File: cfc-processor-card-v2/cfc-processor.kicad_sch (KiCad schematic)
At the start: 6 parts

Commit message: CFC processor schematic Change
changed to hierarchy view, changed all global net labels to hierarchy labels, changed all resistor, capacitor, and ground symbols to modern oresat labels. Deleted connectors sheet and added .history to gitignore.
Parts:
- added J1: TFM-120-01-L-D-RA, oresat-connectors:J-SAMTEC-TFM-120-X1-XXX-D-RA, symbol oresat-connectors:J-SAMTEC-TFM-120-01-L-D-RA
- added J2: 2-1734592-0, oresat-connectors:J-JST-SM14BSHLSTF, symbol oresat-connectors:ORESAT-DEBUG-CONNECTOR-3
- added J3: J-SAMTEC-TFM-110-X1-XXX-D-RA, oresat-connectors:J-SAMTEC-TFM-110-X1-XXX-D-RA, symbol oresat-connectors:J-SAMTEC-TFM-110-01-L-D-RA
- added PCB1: ORESAT-CARD-V1.3-GENERIC-0RF, cfc-card:ORESAT-CARD-V1.3-GENERIC-0RF, symbol cfc-card-eagle-import:ORESAT-CARD-V1.3-GENERIC-0RF
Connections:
- new net: J1.33, J1.34
- new net: J1.35, J1.36
- new net: J1.39, J1.40
- new net C3-UART-RX: J1.38
- new net C3-UART-TX: J1.37
- new net CAN2_H: J1.17, J1.18
- new net CAN2_L: J1.19, J1.20
- new net GND: J1.27, J1.28, J1.29, J1.30, J2.14 (GND), J2.15 (PAD), J2.16 (PAD), J2.5 (GND)
- new net OPD_PWR: J1.15, J1.16
- new net OPD_SCL: J1.13, J1.14
- new net OPD_SDA: J1.11, J1.12
- new net OSD3358: SIP A (PWR)/NRESET: J2.10 (NRST)
- new net OSD3358: SIP B/THERM+: J3.11, J3.12
- new net OSD3358: SIP B/USB_CLI_N: J2.4 (DEVICE-D-)
- new net OSD3358: SIP B/USB_CLI_P: J2.3 (DEVICE-D+)
- new net OSD3358: SIP B/USB_CLI_VBUS: J2.1 (VBUSP), J2.2 (VBUSP)
- new net OSD3358: SIP C/UART-RX: J2.7 (CARD-RX)
- new net OSD3358: SIP C/UART-TX: J2.6 (CARD-TX)
- new net OUT1_N: J3.5, J3.6, J3.7, J3.8
- new net SENSOR_ENABLE: J3.13, J3.14
- new net SPI1_CLK: J3.17, J3.18
- new net SPI1_MISO: J3.15, J3.16
- new net SPI1_MOSI: J3.19, J3.20
- new net TEC_ENABLE: J3.10, J3.9
- new net TXCLK_N: J3.1, J3.2
- new net TXCLK_P: J3.3, J3.4
- new net VBUS: J1.23, J1.24, J1.25, J1.26
- no-connect marks 0 -> 19
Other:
- sheet Connectors renamed Deserializer
- sheet OSD3358: SIP B (USB, XTAL, ADC) renamed OSD3358: SIP B
- sheet OSD3358: SIP C (SD, eMMC, PRU) renamed OSD3358: SIP C
- sheet Deserializer: file cfc-processor-sch-connectors.kicad_sch -> cfc-processor-sch-Deserializer.kicad_sch
- sheet Deserializer ports: added OUT1_N, OUT1_P, PRU_BUS.PRU0_0, PRU_BUS.PRU0_1, PRU_BUS.PRU0_2, PRU_BUS.PRU0_3, PRU_BUS.PRU0_4, PRU_BUS.PRU0_5, PRU_BUS.PRU0_6, PRU_BUS.PRU_16_CLK, TXCLK_N, TXCLK_P; removed none
- sheet OSD3358: SIP A (PWR) ports: added NRESET, VIN_USB; removed none
- sheet OSD3358: SIP B ports: added THERM+, USB_CLI_N, USB_CLI_P, USB_CLI_VBUS, VIN_USB; removed none
- sheet OSD3358: SIP C ports: added CAN2_H, CAN2_L, PRU_BUS.PRU0_0, PRU_BUS.PRU0_1, PRU_BUS.PRU0_2, PRU_BUS.PRU0_3, PRU_BUS.PRU0_4, PRU_BUS.PRU0_5, PRU_BUS.PRU0_6, PRU_BUS.PRU_16_CLK, SPI1_CLK, SPI1_MISO, SPI1_MOSI, UART-RX, UART-TX; removed none
- sheet OSD3358: SIP D (BOOT) ports: added SENSOR_ENABLE, SYSBOOT2, TEC_ENABLE; removed none
- sheet Power (OPD) ports: added C3-UART-RX, C3-UART-TX, OPD_PWR, OPD_SCL, OPD_SDA, SYSBOOT2, UART0_RX, UART0_TX; removed none
- note added: "Aux Bus Connector"
- note added: "CAN1_H"
- note added: "CAN1_L"
- note added: "Main Bus Connector"
- note added: "Oresat Debug Connector"
- note added: "SPARE1"
- note added: "SPARE10"
- note added: "SPARE2"
- note added: "SPARE21"
- note added: "SPARE22"
- note added: "SPARE3"
- note added: "SPARE31"
- note added: "SPARE32"
- note added: "SPARE4"
- note added: "SPARE5"
- note added: "SPARE6"
- note added: "SPARE7"
- note added: "SPARE8"
- note added: "SPARE9"
- note added: "~{SD}"
- moved on the sheet: FID1, FID2, FID3, FID4, FID5, FID6

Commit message: Updated OPD
couple of resistors and caps added to schematic. Changed USB ESD clamp VDD to 3.3v instead of octavo created VDD line.
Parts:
- removed PCB1: ORESAT-CARD-V1.3-GENERIC-0RF, cfc-card:ORESAT-CARD-V1.3-GENERIC-0RF, symbol cfc-card-eagle-import:ORESAT-CARD-V1.3-GENERIC-0RF
- added C56: 10u, oresat-passives:0805-B-NOSILK, symbol Device:C
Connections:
- net GND: now also C56.2
- net VBUS: now also C56.1
- net OSD3358: SIP B/THERM+ renamed THERM+
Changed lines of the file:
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@@
+	)
+	(junction
+		(at 58.42 100.33)
+		(diameter 0)
+		(color 0 0 0 0)
 	)
 	(junction
@@
 	)
 	(junction
+		(at 58.42 90.17)
+		(diameter 0)
+		(color 0 0 0 0)
+	)
+	(junction
 		(at 46.99 90.17)
 		(diameter 0)
@@
 	(wire
 		(pts
+			(xy 58.42 99.06) (xy 58.42 100.33)
+		)
+		(stroke
+			(width 0)
+			(type default)
+		)
+	)
+	(wire
+		(pts
 			(xy 388.62 139.7) (xy 392.43 139.7)
 		)
@@
 	(wire
 		(pts
-			(xy 317.5 132.08) (xy 354.33 132.08)
-		)
-		(stroke
-			(width 0)
-			(type default)
-		)
-	)
-	(wire
-		(pts
-			(xy 321.31 175.26) (xy 321.31 137.16)
+			(xy 316.23 132.08) (xy 354.33 132.08)
+		)
+		(stroke
+			(width 0)
+			(type default)
+		)
+	)
+	(wire
+		(pts
+			(xy 318.77 175.26) (xy 318.77 137.16)
 		)
 		(stroke
@@
 	(wire
 		(pts
-			(xy 325.12 142.24) (xy 356.87 142.24)
+			(xy 321.31 142.24) (xy 356.87 142.24)
 		)
 		(stroke
@@
 	(wire
 		(pts
-			(xy 307.34 175.26) (xy 321.31 175.26)
+			(xy 307.34 175.26) (xy 318.77 175.26)
 		)
 		(stroke
@@
 	(wire
 		(pts
-			(xy 325.12 177.8) (xy 325.12 142.24)
+			(xy 321.31 177.8) (xy 321.31 142.24)
 		)
 		(stroke
@@
 	(wire
 		(pts
-			(xy 307.34 177.8) (xy 325.12 177.8)
+			(xy 307.34 177.8) (xy 321.31 177.8)
 		)
 		(stroke
@@
 	(wire
 		(pts
+			(xy 58.42 90.17) (xy 58.42 91.44)
+		)
+		(stroke
+			(width 0)
+			(type default)
+		)
+	)
+	(wire
+		(pts
 			(xy 39.37 208.28) (xy 50.8 208.28)
 		)
@@
 	(wire
 		(pts
-			(xy 307.34 172.72) (xy 317.5 172.72)
+			(xy 307.34 172.72) (xy 316.23 172.72)
 		)
 		(stroke
@@
 	(wire
 		(pts
-			(xy 321.31 137.16) (xy 356.87 137.16)
+			(xy 318.77 137.16) (xy 356.87 137.16)
 		)
 		(stroke
@@
 	(wire
 		(pts
-			(xy 317.5 172.72) (xy 317.5 132.08)
-		)
-		(stroke
-			(width 0)
-			(type default)
+			(xy 316.23 172.72) (xy 316.23 132.08)
+		)
+		(stroke
+			(width 0)
+			(type default)
+		)
+	)
+	(label "THERM+"
+		(at 379.73 152.4 0)
+		(effects
+			(font
+				(size 1.27 1.27)
+			)
+			(justify left bottom)
 		)
 	)
 	(label "TEC_ENABLE"
-		(at 375.92 147.32 0)
+		(at 374.65 147.32 0)
 		(effects
 			(font
@@
 	)
 	(label "SPI1_MISO"
-		(at 377.19 162.56 0)
+		(at 375.92 162.56 0)
 		(effects
 			(font
@@
 	)
 	(label "SPI1_MOSI"
-		(at 377.19 172.72 0)
+		(at 375.92 172.72 0)
 		(effects
 			(font
@@
 	)
 	(symbol
+		(lib_id "Device:C")
+		(at 58.42 95.25 0)
+		(mirror y)
+		(unit 1)
+		(body_style 1)
+		(exclude_from_sim no)
+		(in_bom yes)
+		(on_board yes)
+		(in_pos_files yes)
+		(dnp no)
+		(property "Reference" "C56"
+			(at 65.024 94.996 0)
+			(show_name no)
+			(do_not_autoplace no)
+			(effects
+				(font
+					(size 1.27 1.27)
+				)
+				(justify left bottom)
+			)
+		)
+		(property "Value" "10u"
+			(at 65.024 97.028 0)
+			(show_name no)
+			(do_not_autoplace no)
+			(effects
+				(font
+					(size 1.27 1.27)
+				)
+				(justify left bottom)
+			)
+		)
+		(property "Footprint" "oresat-passives:0805-B-NOSILK"
+			(at 58.42 95.25 0)
+			(hide yes)
+			(show_name no)
+			(do_not_autoplace no)
+			(effects
+				(font
+					(size 1.27 1.27)
+				)
+			)
+		)
+		(property "Datasheet" "https://mm.digikey.com/Volume0/opasdata/d220001/medias/docus/7851/1276_CL21B1.pdf"
+			(at 58.42 95.25 0)
+			(hide yes)
+			(show_name no)
+			(do_not_autoplace no)
+			(effects
+				(font
+					(size 1.27 1.27)
+				)
+			)
+		)
+		(property "Description" "10 µF ±10% 25V Ceramic Capacitor X7R 0805 (2012 Metric)"
+			(at 58.42 95.25 0)
+			(hide yes)
+			(show_name no)
+			(do_not_autoplace no)
+			(effects
+				(font
+					(size 1.27 1.27)
+				)
+			)
+		)
+		(property "DIS" "DigiKey"
+			(at 58.42 95.25 0)
+			(hide yes)
+			(show_name no)
+			(do_not_autoplace no)
+			(effects
+				(font
+					(size 1.27 1.27)
+				)
+			)
+		)
+		(property "DPN" "1276-CL21B106KAYQNNETR-ND"
+			(at 58.42 95.25 0)
+			(hide yes)
+			(show_name no)
+			(do_not_autoplace no)
+			(effects
+				(font
+					(size 1.27 1.27)
+				)
+			)
+		)
+		(property "MFR" "Samsung Electro-Mechanics"
+			(at 58.42 95.25 0)
+			(hide yes)
+			(show_name no)
+			(do_not_autoplace no)
+			(effects
+				(font
+					(size 1.27 1.27)
+				)
+			)
+		)
+		(property "MPN" "CL21B106KAYQNNE"
+			(at 58.42 95.25 0)
+			(hide yes)
+			(show_name no)
+			(do_not_autoplace no)
+			(effects
+				(font
+					(size 1.27 1.27)
+				)
+			)
+		)
+		(pin "1"
+		)
+		(pin "2"
+		)
+		(instances
+			(project "cfc-processor"
+				(path "/07ac832f-8d98-4777-b655-1877592dfd88"
+					(reference "C56")
+					(unit 1)
+				)
+			)
+		)
+	)
+	(symbol
 		(lib_name "Fiducial_4")
 		(lib_id "Mechanical:Fiducial")
@@
 					(unit 1)
 				)
-			)
-		)
-	)
-	(symbol
-		(lib_id "cfc-card-eagle-import:ORESAT-CARD-V1.3-GENERIC-0RF")
-		(at 16.51 248.92 0)
-		(unit 1)
-		(body_style 1)
-		(exclude_from_sim no)
-		(in_bom yes)
-		(on_board yes)
-		(in_pos_files yes)
-		(dnp no)
-		(property "Reference" "PCB1"
-			(at 16.51 248.92 0)
-			(hide yes)
-			(show_name no)
-			(do_not_autoplace no)
-			(effects
-				(font
-					(size 1.27 1.27)
-				)
-			)
-		)
-		(property "Value" "ORESAT-CARD-V1.3-GENERIC-0RF"
-			(at 16.51 248.92 0)
-			(hide yes)
-			(show_name no)
-			(do_not_autoplace no)
-			(effects
-				(font
-					(size 1.27 1.27)
-				)
-			)
-		)
-		(property "Footprint" "cfc-card:ORESAT-CARD-V1.3-GENERIC-0RF"
-			(at 16.51 248.92 0)
-			(hide yes)
-			(show_name no)
-			(do_not_autoplace no)
-			(effects
-				(font
-					(size 1.27 1.27)
-				)
-			)
-		)
-		(property "Datasheet" "N/A"
-			(at 16.51 248.92 0)
-			(hide yes)
-			(show_name no)
-			(do_not_autoplace no)
-			(effects
-				(font
-					(size 1.27 1.27)
-				)
-			)
-		)
-		(property "Description" "N/A"
-			(at 16.51 248.92 0)
-			(hide yes)
-			(show_name no)
-			(do_not_autoplace no)
-			(effects
-				(font
-					(size 1.27 1.27)
-				)
-			)
-		)
-		(property "DIS" "N/A"
-			(at 16.51 248.92 0)
-			(hide yes)
-			(show_name no)
-			(do_not_autoplace no)
-			(effects
-				(font
-					(size 1.27 1.27)
-				)
-			)
-		)
-		(property "DPN" "N/A"
-			(at 16.51 248.92 0)
-			(hide yes)
-			(show_name no)
-			(do_not_autoplace no)
-			(effects
-				(font
-					(size 1.27 1.27)
-				)
-			)
-		)
-		(property "MFR" "N/A"
-			(at 16.51 248.92 0)
-			(hide yes)
-			(show_name no)
-			(do_not_autoplace no)
-			(effects
-				(font
-					(size 1.27 1.27)
-				)
-			)
-		)
-		(property "MPN" "N/A"
-			(at 16.51 248.92 0)
-			(hide yes)
-			(show_name no)
-			(do_not_autoplace no)
-			(effects
-				(font
-					(size 1.27 1.27)
-				)
-			)
-		)
-		(instances
-			(project "cfc-processor"
-				(path "/07ac832f-8d98-4777-b655-1877592dfd88"
-					(reference "PCB1")
-					(unit 1)
-				)

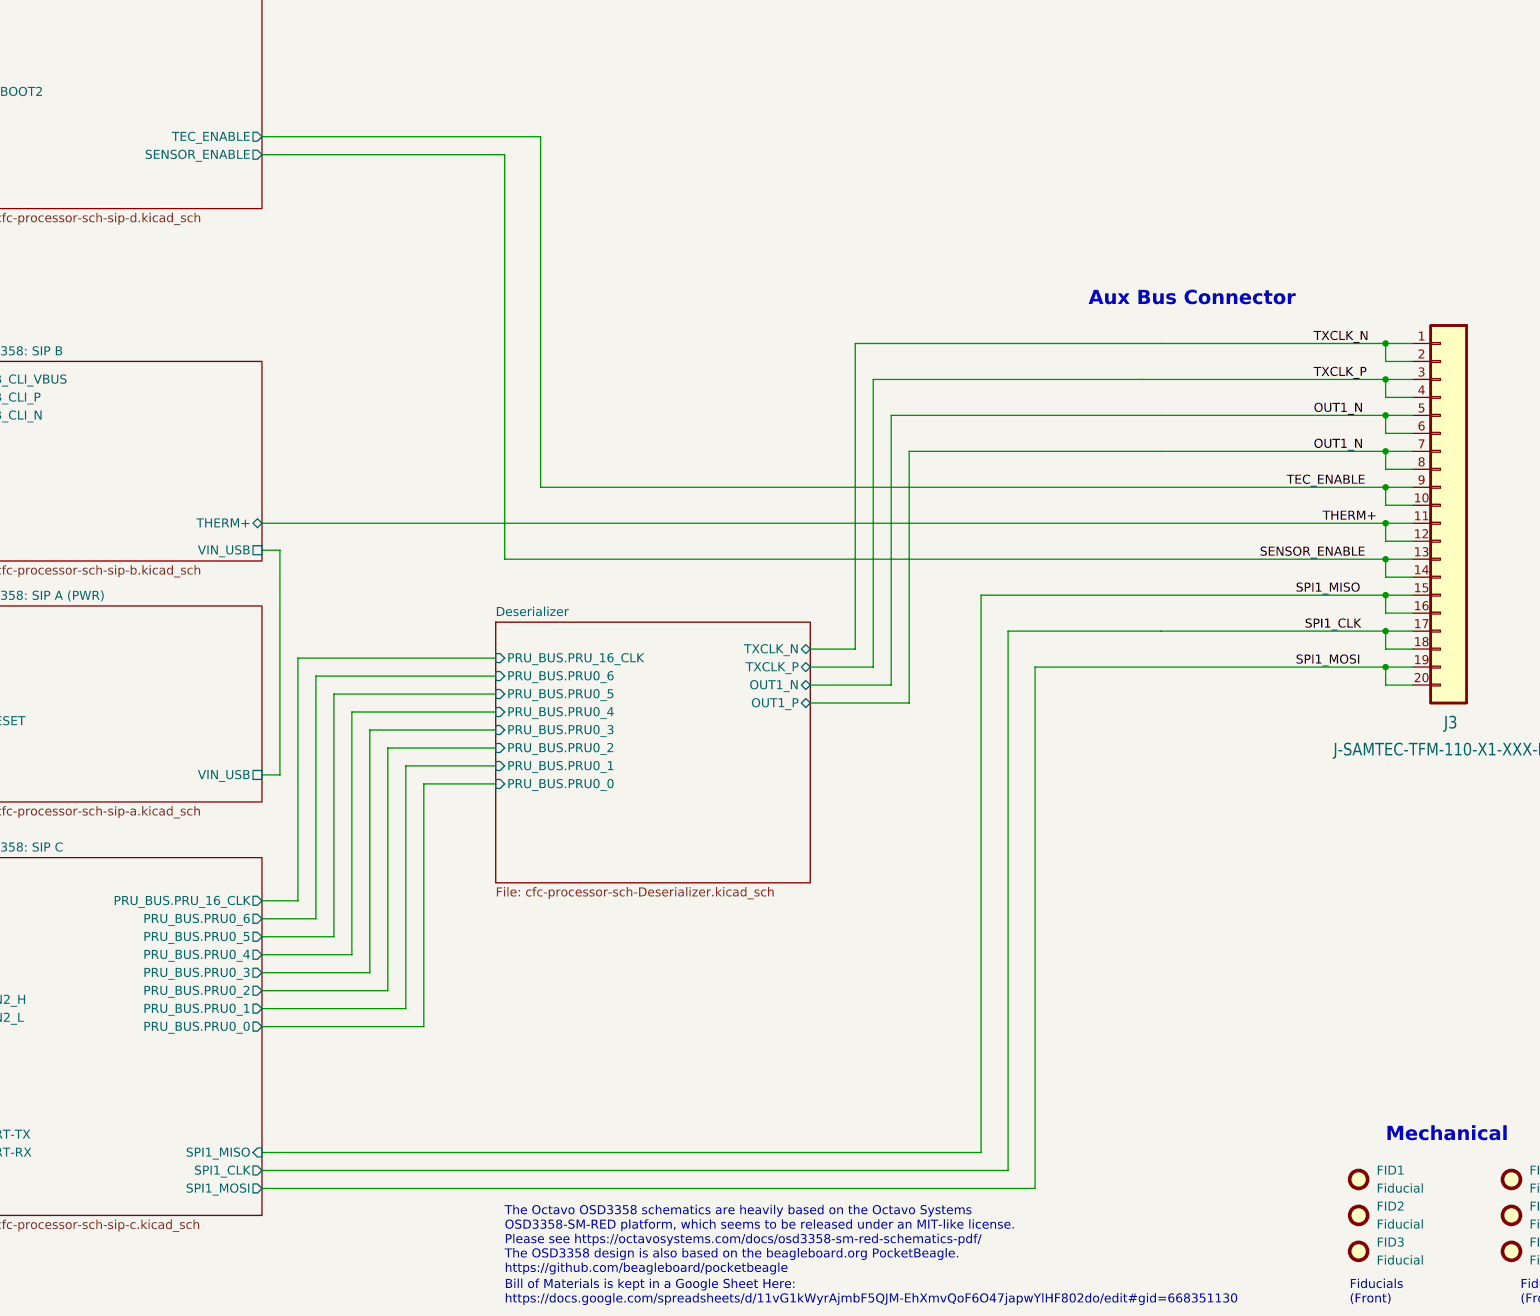
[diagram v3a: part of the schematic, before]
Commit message: Update
Added pull down resistors and removed therm + and sensor enable and added i2c support for cfc sensor card.
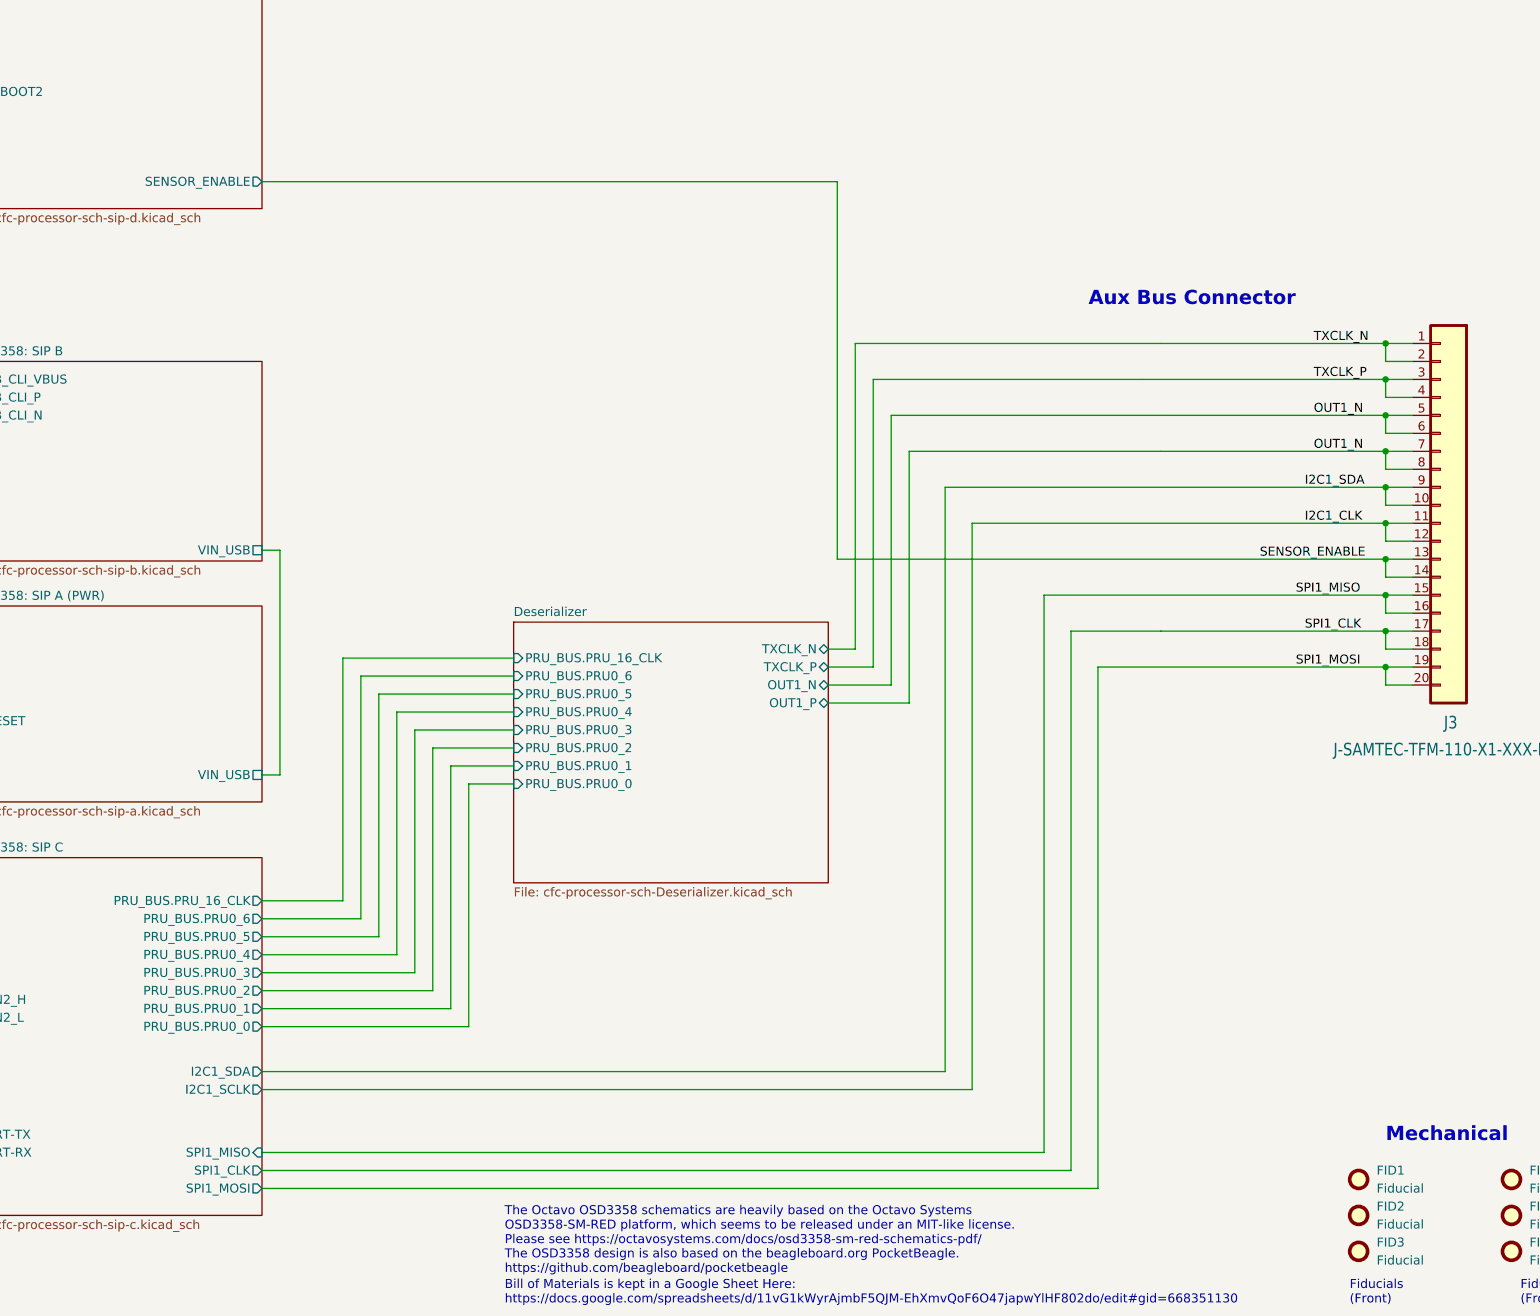
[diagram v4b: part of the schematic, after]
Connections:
- net TEC_ENABLE renamed I2C1_SDA
- net THERM+ renamed I2C1_CLK
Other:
- sheet OSD3358: SIP B ports: added none; removed THERM+
- sheet OSD3358: SIP C ports: added I2C1_SCLK, I2C1_SDA; removed none
- sheet OSD3358: SIP D (BOOT) ports: added none; removed TEC_ENABLE

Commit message: Update
Fixed a couple of library issues on testpoints and other misc components. Added Pull up resistors to 8 channel i2c ic
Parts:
- added J4: Conn_01x04, Connector_PinHeader_2.54mm:PinHeader_1x04_P2.54mm_Vertical, symbol Connector_Generic:Conn_01x04
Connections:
- net GND: now also J4.4 (Pin_4)
- net SENSOR_ENABLE: no longer names the net of J3.13, J3.14
- new net EEPROM_WP: J4.3 (Pin_3)
- new net I2C0_SCL: J4.1 (Pin_1)
- new net I2C0_SDA: J4.2 (Pin_2)
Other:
- sheet OSD3358: SIP A (PWR) ports: added EEPROM_WP, I2C0_SCL, I2C_SDA; removed none
- note added: "EEPROM Programming Jumper Pull Pin 3 low to write to EEPROM. Use Raspberry Pi Pico board with Circuit Python software to program. Careful with ESD!"
